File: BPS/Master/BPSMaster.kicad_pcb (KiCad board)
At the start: 2 copper layers, 100 x 75 mm, 142 parts, among them J1 SWD, J10 CurrentSlaveConnector, J11 USB_B_Micro, J13 CAN Analyzer, J2 CarPowerConnector, J3 FrontFans, J4 BackFans, J5 SPI Analyzer, J6 VoltageSlaveConnector, J7 ContactorConnector, J8 CAN_Out, J9 ErrorLightConnector, Q1 VND5N07-E, Q2 NTR4003NT1G, Q3 NTR4003NT1G, Q4 NTR4003NT1G, SW1 B3SL-1002P, U1 STM32F413RHTx, U10 BAS70-04, U11 SI8261ABC-IS, U12 CDSOT23-T24CAN, U13 ADM3055E, U14 SI8261ABC-IS, U15 CP2102N-A01-GQFN24, U2 RI3-1205S, U3 NCP1117-3.3_SOT223, U4 M24128, U5 LTC6256, U8 LTC6820, U9 HX1188FNL, Y1 8M

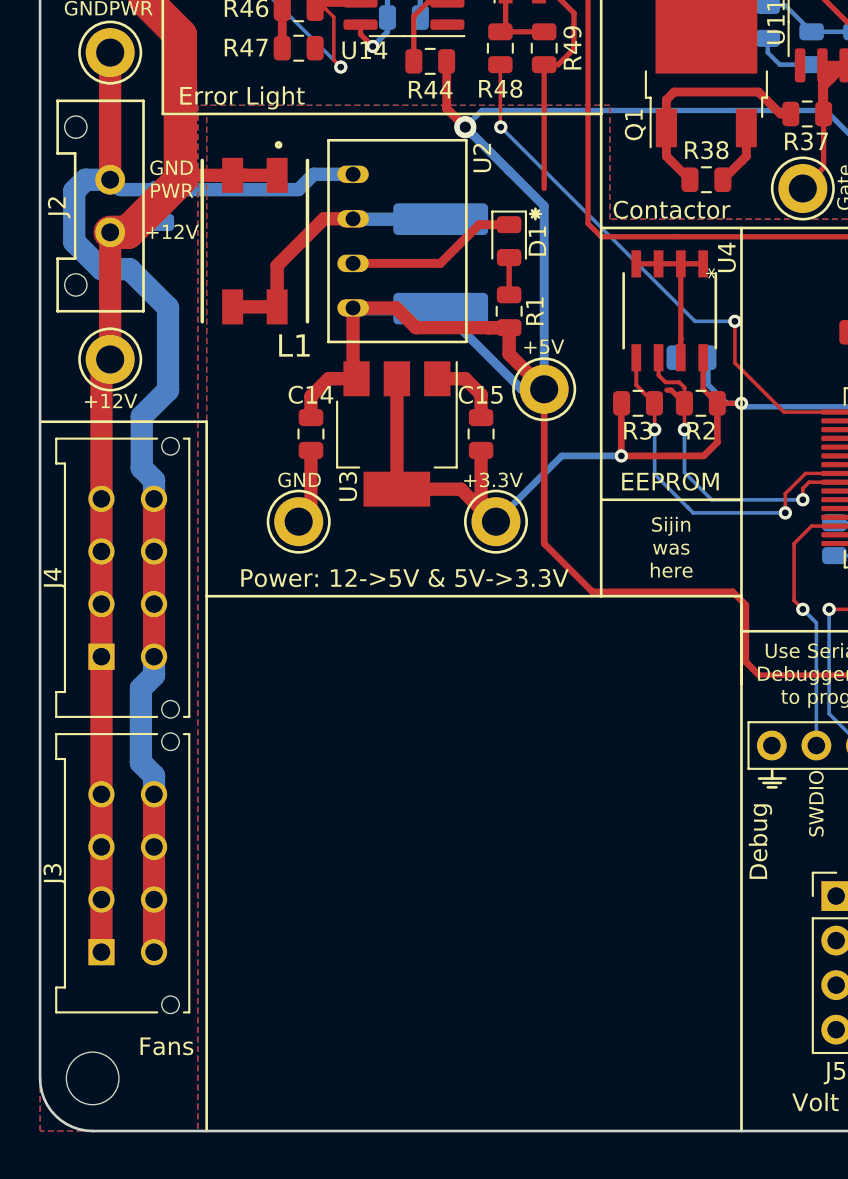
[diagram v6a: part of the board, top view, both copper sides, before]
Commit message: Adds resistor mount. Need to add pheonix connector.
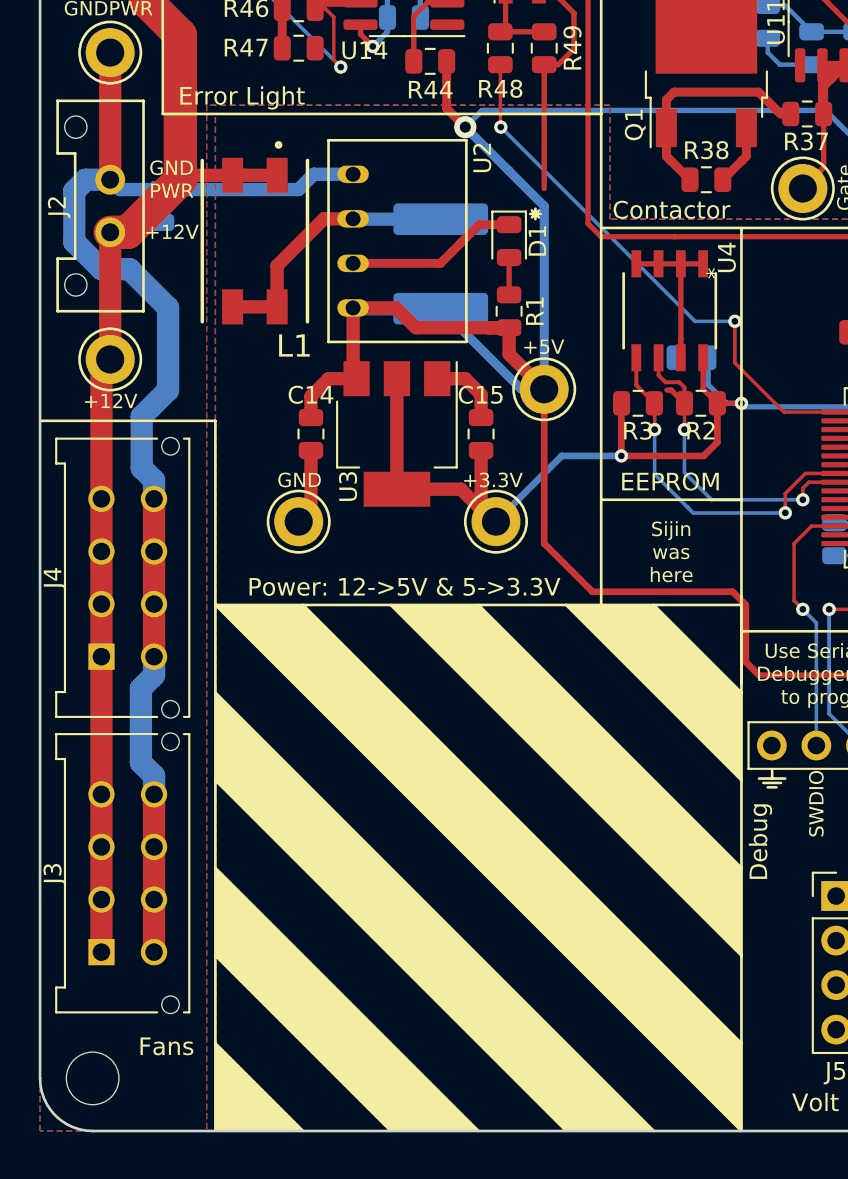
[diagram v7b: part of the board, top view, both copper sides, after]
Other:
- board text added: "Power: 12->5V & 5->3.3V"
- board text removed: "Power: 12->5V & 5V->3.3V"
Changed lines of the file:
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@@
   (general
     (thickness 1.6)
-    (drawings 183)
+    (drawings 208)
     (tracks 993)
     (zones 0)
@@
     (45 Margin user)
     (46 B.CrtYd user hide)
-    (47 F.CrtYd user)
+    (47 F.CrtYd user hide)
     (48 B.Fab user hide)
     (49 F.Fab user hide)
@@
       (net 2 +3V3))
   )
+  (gr_poly (pts (xy 115 150) (xy 110 150) (xy 110 145)) (layer B.SilkS) (width 0.1))
+  (gr_poly (pts (xy 125 150) (xy 120 150) (xy 110 140) (xy 110 135)) (layer B.SilkS) (width 0.1))
+  (gr_poly (pts (xy 135 150) (xy 130 150) (xy 110 130) (xy 110 125)) (layer B.SilkS) (width 0.1))
+  (gr_poly (pts (xy 140 145) (xy 140 150) (xy 110 120) (xy 115 120)) (layer B.SilkS) (width 0.1))
+  (gr_poly (pts (xy 140 135) (xy 140 140) (xy 120 120) (xy 125 120)) (layer B.SilkS) (width 0.1))
+  (gr_poly (pts (xy 140 125) (xy 140 130) (xy 130 120) (xy 135 120)) (layer B.SilkS) (width 0.1))
+  (gr_poly (pts (xy 140 125) (xy 140 130) (xy 130 120) (xy 135 120)) (layer F.SilkS) (width 0.1))
+  (gr_poly (pts (xy 140 135) (xy 140 140) (xy 120 120) (xy 125 120)) (layer F.SilkS) (width 0.1))
+  (gr_poly (pts (xy 140 145) (xy 140 150) (xy 110 120) (xy 115 120)) (layer F.SilkS) (width 0.1))
+  (gr_poly (pts (xy 135 150) (xy 130 150) (xy 110 130) (xy 110 125)) (layer F.SilkS) (width 0.1))
+  (gr_poly (pts (xy 125 150) (xy 120 150) (xy 110 140) (xy 110 135)) (layer F.SilkS) (width 0.1))
+  (gr_poly (pts (xy 115 150) (xy 110 150) (xy 110 145)) (layer F.SilkS) (width 0.1))
+  (gr_line (start 110 145) (end 115 150) (layer F.SilkS) (width 0.15))
+  (gr_line (start 120 150) (end 110 140) (layer F.SilkS) (width 0.15))
+  (gr_line (start 110 135) (end 125 150) (layer F.SilkS) (width 0.15))
+  (gr_line (start 130 150) (end 110 130) (layer F.SilkS) (width 0.15))
+  (gr_line (start 110 125) (end 135 150) (layer F.SilkS) (width 0.15))
+  (gr_line (start 140 125) (end 135 120) (layer F.SilkS) (width 0.15))
+  (gr_line (start 130 120) (end 140 130) (layer F.SilkS) (width 0.15))
+  (gr_line (start 140 135) (end 125 120) (layer F.SilkS) (width 0.15))
+  (gr_line (start 120 120) (end 140 140) (layer F.SilkS) (width 0.15))
+  (gr_line (start 140 145) (end 115 120) (layer F.SilkS) (width 0.15))
+  (gr_line (start 110 120) (end 140 150) (layer F.SilkS) (width 0.15))
+  (gr_text EEPROM (at 135.95 113) (layer B.SilkS)
+    (effects (font (size 1 1) (thickness 0.15)) (justify mirror))
+  )
+  (gr_line (start 140 114) (end 132 114) (layer B.SilkS) (width 0.15))
   (gr_text "GND\nPWR" (at 107.5 95.75) (layer F.SilkS)
     (effects (font (size 0.8128 0.8128) (thickness 0.1524)))
@@
     (effects (font (size 0.8128 0.8128) (thickness 0.1524)) (justify mirror))
   )
-  (gr_text "WARNING! GNDPWR and GND\nare isolated from each other" (at 111.5 104 90) (layer B.SilkS)
+  (gr_text "WARNING! GNDPWR and GND\nare isolated from each other" (at 112 104 90) (layer B.SilkS)
     (effects (font (size 1 1) (thickness 0.15)) (justify mirror))
   )
@@
     (effects (font (size 1 1) (thickness 0.15)) (justify mirror))
   )
-  (gr_text "Power: 12->5V & 5V->3.3V" (at 120.75 118.5) (layer B.SilkS)
+  (gr_text "Power: 12->5V & 5->3.3V" (at 120.75 119) (layer B.SilkS)
     (effects (font (size 1 1) (thickness 0.15)) (justify mirror))
   )
@@
   (gr_line (start 168 121.5) (end 168 150) (layer B.SilkS) (width 0.15))
   (gr_line (start 151 121.5) (end 168 121.5) (layer B.SilkS) (width 0.15))
-  (gr_line (start 140 119.5) (end 140 98.5) (layer B.SilkS) (width 0.15))
+  (gr_line (start 140 120) (end 140 98.5) (layer B.SilkS) (width 0.15))
   (gr_line (start 151 121.5) (end 140 121.5) (layer B.SilkS) (width 0.15))
   (gr_line (start 151 150) (end 151 121.5) (layer B.SilkS) (width 0.15))
   (gr_line (start 140 119.5) (end 140 150) (layer B.SilkS) (width 0.15))
-  (gr_line (start 132 119.5) (end 140 119.5) (layer B.SilkS) (width 0.15))
-  (gr_line (start 109.5 119.5) (end 109.5 150) (layer B.SilkS) (width 0.15))
-  (gr_line (start 109.5 109.5) (end 100 109.5) (layer B.SilkS) (width 0.15))
-  (gr_line (start 109.5 119.5) (end 109.5 109.5) (layer B.SilkS) (width 0.15))
-  (gr_line (start 132 119.5) (end 109.5 119.5) (layer B.SilkS) (width 0.15))
-  (gr_line (start 132 98.5) (end 132 119.5) (layer B.SilkS) (width 0.15))
+  (gr_line (start 132 120) (end 140 120) (layer B.SilkS) (width 0.15))
+  (gr_line (start 110 119.5) (end 110 150) (layer B.SilkS) (width 0.15))
+  (gr_line (start 110 109.5) (end 100 109.5) (layer B.SilkS) (width 0.15))
+  (gr_line (start 110 119.5) (end 110 109.5) (layer B.SilkS) (width 0.15))
+  (gr_line (start 132 120) (end 110 120) (layer B.SilkS) (width 0.15))
+  (gr_line (start 132 98.5) (end 132 120) (layer B.SilkS) (width 0.15))
   (gr_line (start 107 92) (end 132 92) (layer B.SilkS) (width 0.15))
   (gr_line (start 107 75) (end 107 92) (layer B.SilkS) (width 0.15))
@@
     (effects (font (size 0.8128 0.8128) (thickness 0.1524)) (justify right))
   )
-  (gr_text "Sijin\nwas\nhere" (at 136 116.75) (layer F.SilkS)
+  (gr_text "Sijin\nwas\nhere" (at 136 117) (layer F.SilkS)
     (effects (font (size 0.8128 0.8128) (thickness 0.1524)))
   )
@@
   )
   (gr_line (start 140 119.5) (end 140 98.5) (layer F.SilkS) (width 0.15))
-  (gr_text "Power: 12->5V & 5V->3.3V" (at 120.75 118.5) (layer F.SilkS)
+  (gr_text "Power: 12->5V & 5->3.3V" (at 120.75 119) (layer F.SilkS)
     (effects (font (size 1 1) (thickness 0.15)))
   )
-  (gr_line (start 132 98.5) (end 132 119.5) (layer F.SilkS) (width 0.15))
+  (gr_line (start 132 98.5) (end 132 120) (layer F.SilkS) (width 0.15))
   (gr_text "Error Light" (at 111.5 91) (layer F.SilkS)
     (effects (font (size 1 1) (thickness 0.15)))
@@
     (effects (font (size 0.8128 0.8128) (thickness 0.1524)))
   )
-  (gr_line (start 109.5 109.55) (end 100 109.55) (layer F.SilkS) (width 0.15))
-  (gr_line (start 140 119.5) (end 109.5 119.5) (layer F.SilkS) (width 0.15))
+  (gr_line (start 110 109.5) (end 100 109.5) (layer F.SilkS) (width 0.15))
+  (gr_line (start 140 120) (end 110 120) (layer F.SilkS) (width 0.15))
   (gr_line (start 140 124.5) (end 140 119.5) (layer F.SilkS) (width 0.15))
   (gr_line (start 179.5 98.5) (end 200 98.5) (layer F.SilkS) (width 0.15))
   (gr_line (start 200 86) (end 179.5 86) (layer F.SilkS) (width 0.15))
   (gr_line (start 140 150) (end 140 120) (layer F.SilkS) (width 0.15))
-  (gr_line (start 109.5 150) (end 109.5 109.55) (layer F.SilkS) (width 0.15))
+  (gr_line (start 110 149.95) (end 110 109.5) (layer F.SilkS) (width 0.15))
   (gr_line (start 100.5 100.5) (end 101 100) (layer F.Fab) (width 0.15))
   (gr_line (start 100 100) (end 100.5 100.5) (layer F.Fab) (width 0.15))
@@
         (xy 157.5 75) (xy 200 75) (xy 200 121.5) (xy 177 121.5) (xy 177 150)
         (xy 168 150) (xy 168 131.5) (xy 151 131.5) (xy 151 150) (xy 140 150)
-        (xy 122 150) (xy 109.5 150) (xy 109.5 92) (xy 132 92) (xy 132 98.5)
+        (xy 122 150) (xy 110 150) (xy 110 92) (xy 132 92) (xy 132 98.5)
         (xy 157.5 98.5)
       )
@@
     (polygon
       (pts
-        (xy 157 75) (xy 157 98) (xy 132.5 98) (xy 132.5 91.5) (xy 109 91.5)
-        (xy 109 150) (xy 100 150) (xy 100 75)
+        (xy 157 75) (xy 157 98) (xy 132.5 98) (xy 132.5 91.5) (xy 109.5 91.5)
+        (xy 109.5 150) (xy 100 150) (xy 100 75)
       )
     )
@@
         (xy 157.5 75) (xy 200 75) (xy 200 121.5) (xy 177 121.5) (xy 177 150)
         (xy 168 150) (xy 168 131.5) (xy 151 131.5) (xy 151 150) (xy 140 150)
-        (xy 122 150) (xy 109.5 150) (xy 109.5 92) (xy 132 92) (xy 132 98.5)
+        (xy 122 150) (xy 110 150) (xy 110 92) (xy 132 92) (xy 132 98.5)
         (xy 157.5 98.5)
       )
@@
     (polygon
       (pts
-        (xy 157 98) (xy 132.5 98) (xy 132.5 91.5) (xy 109 91.5) (xy 109 150)
+        (xy 157 98) (xy 132.5 98) (xy 132.5 91.5) (xy 109.5 91.5) (xy 109.5 150)
         (xy 100 150) (xy 100 82) (xy 115.5 82) (xy 140 82) (xy 140 75)
         (xy 157 75)

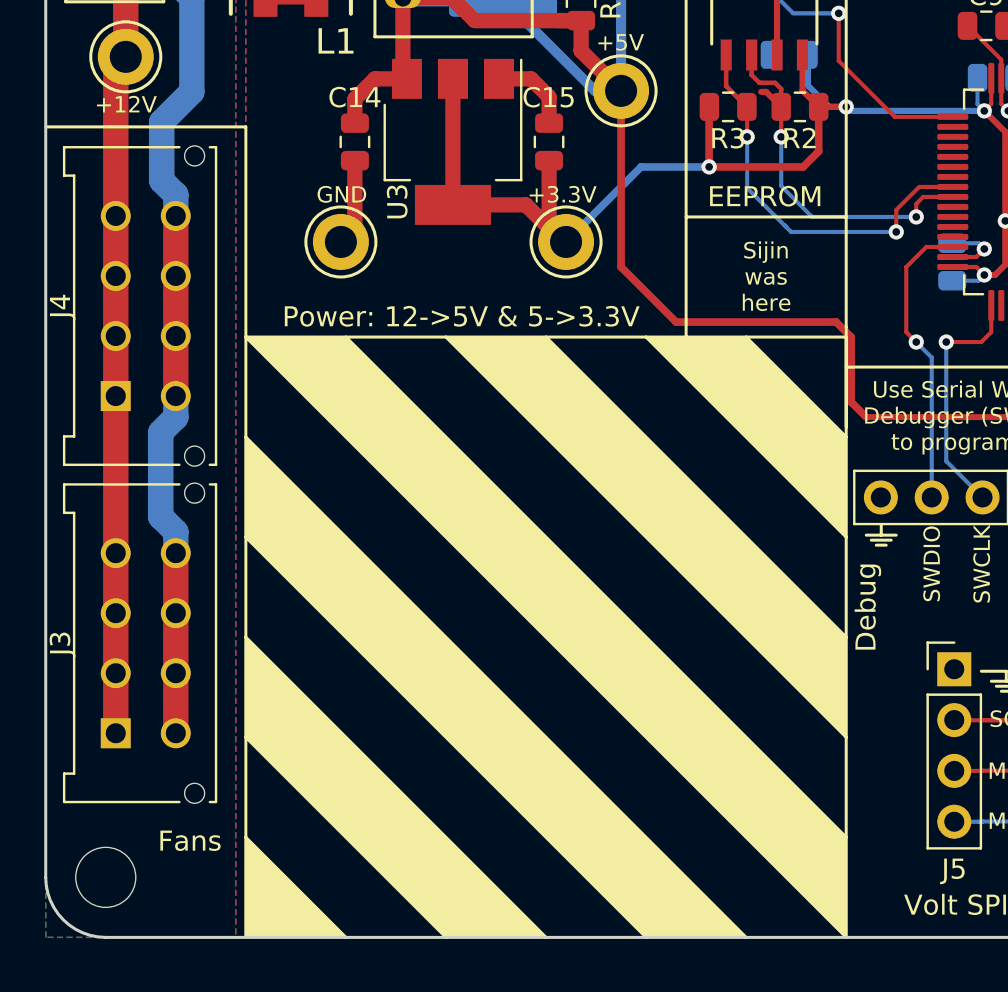
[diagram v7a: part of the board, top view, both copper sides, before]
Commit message: Adds final BPS leader board and completed Contactor/precharge board.
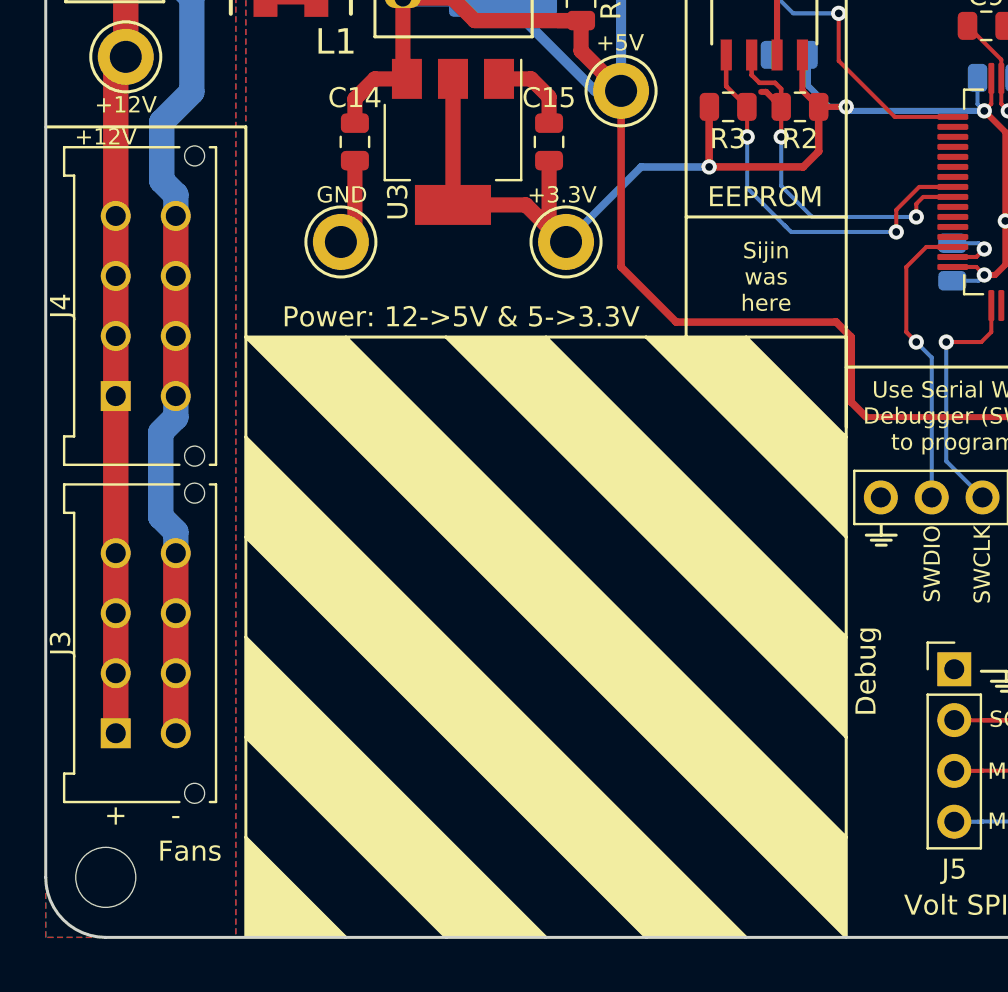
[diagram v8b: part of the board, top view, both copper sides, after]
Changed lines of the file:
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@@
   (general
     (thickness 1.6)
-    (drawings 208)
+    (drawings 211)
     (tracks 993)
     (zones 0)
@@
       (drillshape 0)
       (scaleselection 1)
-      (outputdirectory "../Master_v1.1GRB/"))
+      (outputdirectory "../GerberFiles/Leader/"))
   )
   (net 0 "")
@@
       (net 2 +3V3))
   )
+  (gr_text - (at 106.5 143.9) (layer F.SilkS)
+    (effects (font (size 1 1) (thickness 0.15)))
+  )
+  (gr_text + (at 103.5 143.9) (layer F.SilkS)
+    (effects (font (size 1 1) (thickness 0.15)))
+  )
+  (gr_text +12V (at 103 110) (layer F.SilkS)
+    (effects (font (size 0.8128 0.8128) (thickness 0.1524)))
+  )
   (gr_poly (pts (xy 115 150) (xy 110 150) (xy 110 145)) (layer B.SilkS) (width 0.1))
   (gr_poly (pts (xy 125 150) (xy 120 150) (xy 110 140) (xy 110 135)) (layer B.SilkS) (width 0.1))
@@
     (effects (font (size 1.143 1.143) (thickness 0.15875)) (justify mirror))
   )
-  (gr_text Fans (at 107.2 145.25) (layer B.SilkS)
+  (gr_text Fans (at 107.2 145.75) (layer B.SilkS)
     (effects (font (size 1 1) (thickness 0.15)) (justify mirror))
   )
@@
     (effects (font (size 1 1) (thickness 0.15)) (justify mirror))
   )
-  (gr_text Debug (at 141 133.5 90) (layer B.SilkS)
+  (gr_text Debug (at 141 136.7 90) (layer B.SilkS)
     (effects (font (size 1 1) (thickness 0.15)) (justify mirror))
   )
@@
   (gr_line (start 148 136.7) (end 148 137.2) (layer F.SilkS) (width 0.15))
   (gr_line (start 146.75 136.7) (end 148 136.7) (layer F.SilkS) (width 0.15))
-  (gr_text Debug (at 141 133.5 90) (layer F.SilkS)
+  (gr_text Debug (at 141 136.7 90) (layer F.SilkS)
     (effects (font (size 1 1) (thickness 0.15)))
   )
@@
     (effects (font (size 1 1) (thickness 0.15)))
   )
-  (gr_text Fans (at 107.2 145.2) (layer F.SilkS)
+  (gr_text Fans (at 107.2 145.7) (layer F.SilkS)
     (effects (font (size 1 1) (thickness 0.15)))
   )
@@
   (segment (start 182.45 89.3) (end 182.45 89.95) (width 0.2032) (layer F.Cu) (net 86))
   (zone (net 8) (net_name +12V) (layer F.Cu) (hatch edge 0.508)
-    (connect_pads (clearance 0.254))
+    (connect_pads yes (clearance 0.254))
     (min_thickness 0.127)
     (fill yes (arc_segments 32) (thermal_gap 0.508) (thermal_bridge_width 0.508))
@@
   )
   (zone (net 1) (net_name GND) (layer F.Cu) (hatch edge 0.508)
-    (connect_pads (clearance 0.254))
+    (connect_pads yes (clearance 0.254))
     (min_thickness 0.1524)
     (fill yes (arc_segments 32) (thermal_gap 0.508) (thermal_bridge_width 0.508))
@@
   )
   (zone (net 9) (net_name GNDPWR) (layer B.Cu) (hatch edge 0.508)
-    (connect_pads (clearance 0.254))
+    (connect_pads yes (clearance 0.254))
     (min_thickness 0.127)
     (fill yes (arc_segments 32) (thermal_gap 0.508) (thermal_bridge_width 0.508))
@@
   )
   (zone (net 1) (net_name GND) (layer B.Cu) (hatch edge 0.508)
-    (connect_pads (clearance 0.254))
+    (connect_pads yes (clearance 0.254))
     (min_thickness 0.1524)
     (fill yes (arc_segments 32) (thermal_gap 0.508) (thermal_bridge_width 0.508))
@@
   )
   (zone (net 9) (net_name GNDPWR) (layer F.Cu) (hatch edge 0.508)
-    (connect_pads (clearance 0.254))
+    (connect_pads yes (clearance 0.254))
     (min_thickness 0.127)
     (fill yes (arc_segments 32) (thermal_gap 0.508) (thermal_bridge_width 0.508))
